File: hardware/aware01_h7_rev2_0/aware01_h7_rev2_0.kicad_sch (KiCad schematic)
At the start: 46 parts, among them J1 Conn_02x07_Odd_Even, J2 Conn_02x05_Odd_Even, SW3 PTS815, U1 LMR50410Y5FQDBVRQ1, U2 LM1117MP-3.3, U4 STM32H7A3RITx, U5 LM4040DIM3X-10, Y1 WE-XTAL 24.0MHz 50ppm

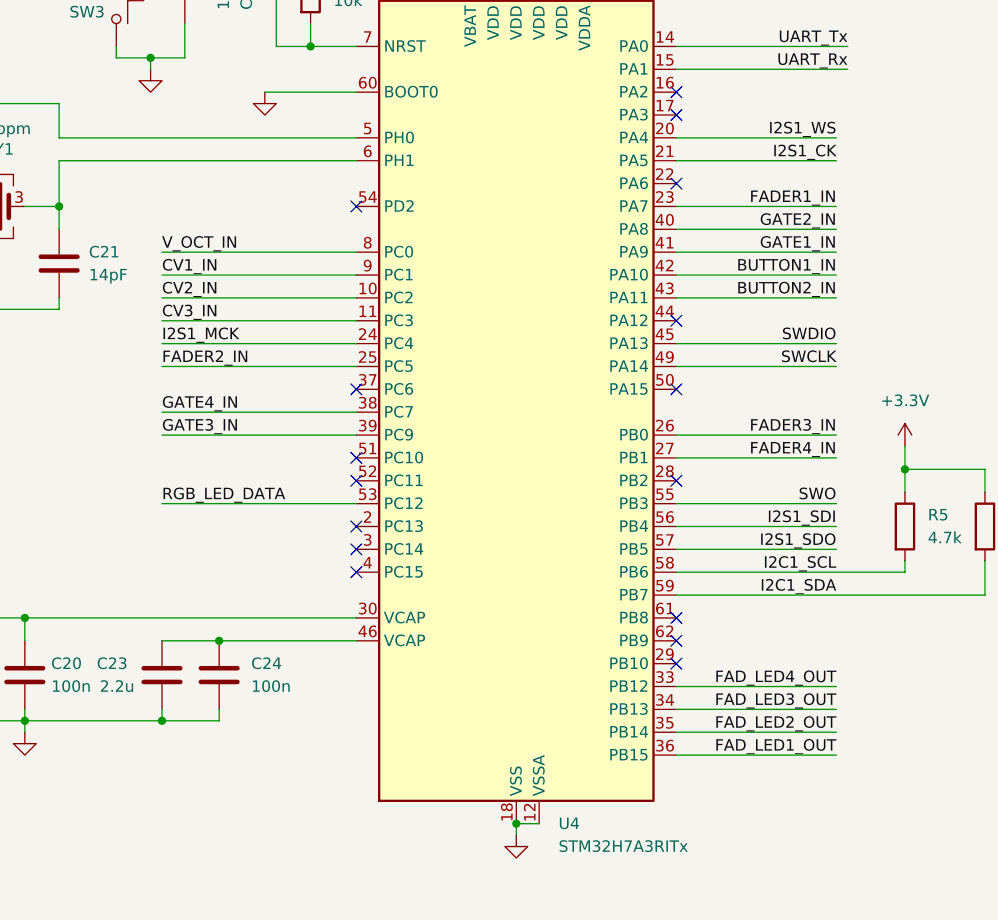
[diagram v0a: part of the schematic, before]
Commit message: feat: fixes in pcb design
- use correct BAT54S placement/layout
- fix pin mapping of fade potentiometers, also adjust routing
- switch pins that did not support PWM out (for fader led)
- switch pins that did not support EXTI
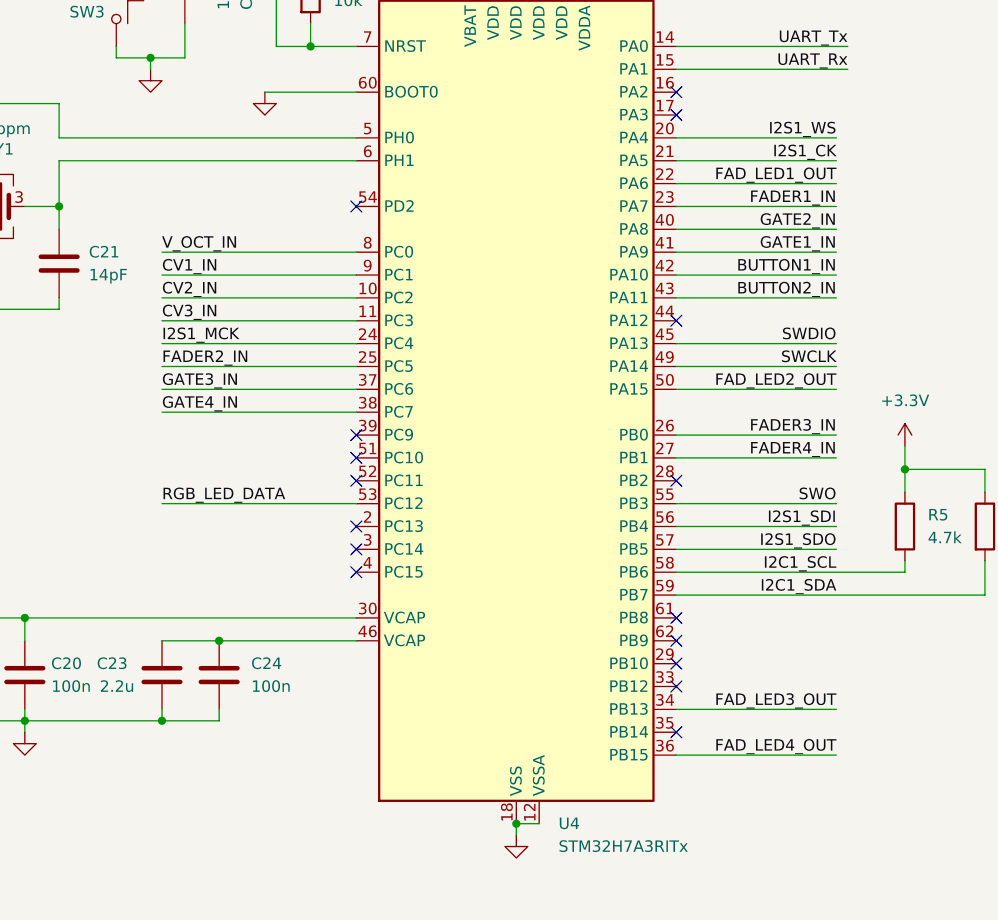
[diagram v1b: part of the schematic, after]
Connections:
- net FAD_LED1_OUT: now also U4.22 (PA6); no longer U4.36 (PB15)
- net FAD_LED2_OUT: now also U4.50 (PA15); no longer U4.35 (PB14)
- net FAD_LED4_OUT: now also U4.36 (PB15); no longer U4.33 (PB12)
- net GATE3_IN: now also U4.37 (PC6); no longer U4.39 (PC9)
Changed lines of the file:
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@@
+	)
+	(no_connect
+		(at 200.66 156.21)
 	)
 	(no_connect
@@
 	)
 	(no_connect
-		(at 236.22 128.27)
-	)
-	(no_connect
 		(at 64.77 237.49)
 	)
@@
 	)
 	(no_connect
+		(at 236.22 176.53)
+	)
+	(no_connect
 		(at 236.22 120.65)
 	)
@@
 	)
 	(no_connect
-		(at 236.22 181.61)
-	)
-	(no_connect
 		(at 236.22 143.51)
 	)
@@
 	)
 	(no_connect
-		(at 236.22 176.53)
+		(at 236.22 184.15)
 	)
 	(no_connect
@@
 	)
 	(no_connect
-		(at 236.22 151.13)
+		(at 236.22 189.23)
+	)
+	(no_connect
+		(at 236.22 181.61)
 	)
 	(no_connect
@@
 	)
 	(no_connect
-		(at 200.66 151.13)
-	)
-	(no_connect
 		(at 200.66 130.81)
 	)
@@
 	(wire
 		(pts
-			(xy 179.07 156.21) (xy 200.66 156.21)
-		)
-		(stroke
-			(width 0)
-			(type default)
-		)
-	)
-	(wire
-		(pts
 			(xy 46.99 40.64) (xy 34.29 40.64)
 		)
@@
 	(wire
 		(pts
+			(xy 179.07 151.13) (xy 200.66 151.13)
+		)
+		(stroke
+			(width 0)
+			(type default)
+		)
+	)
+	(wire
+		(pts
 			(xy 105.41 245.11) (xy 105.41 247.65)
 		)
@@
 	(wire
 		(pts
+			(xy 254 191.77) (xy 236.22 191.77)
+		)
+		(stroke
+			(width 0)
+			(type default)
+		)
+	)
+	(wire
+		(pts
 			(xy 34.29 48.26) (xy 34.29 50.8)
 		)
@@
 	(wire
 		(pts
+			(xy 254 128.27) (xy 236.22 128.27)
+		)
+		(stroke
+			(width 0)
+			(type default)
+		)
+	)
+	(wire
+		(pts
 			(xy 127 39.37) (xy 127 41.91)
 		)
@@
 	(wire
 		(pts
-			(xy 254 191.77) (xy 236.22 191.77)
-		)
-		(stroke
-			(width 0)
-			(type default)
-		)
-	)
-	(wire
-		(pts
 			(xy 48.26 245.11) (xy 52.07 245.11)
 		)
@@
 	(wire
 		(pts
+			(xy 254 151.13) (xy 236.22 151.13)
+		)
+		(stroke
+			(width 0)
+			(type default)
+		)
+	)
+	(wire
+		(pts
 			(xy 236.22 115.57) (xy 255.27 115.57)
 		)
@@
 	(wire
 		(pts
-			(xy 254 189.23) (xy 236.22 189.23)
-		)
-		(stroke
-			(width 0)
-			(type default)
-		)
-	)
-	(wire
-		(pts
 			(xy 133.35 41.91) (xy 127 41.91)
 		)
@@
 		(pts
 			(xy 105.41 252.73) (xy 105.41 250.19)
-		)
-		(stroke
-			(width 0)
-			(type default)
-		)
-	)
-	(wire
-		(pts
-			(xy 254 184.15) (xy 236.22 184.15)
 		)
 		(stroke
@@
 		)
 	)
+	(label "FAD_LED1_OUT"
+		(at 254 128.27 180)
+		(effects
+			(font
+				(size 1.27 1.27)
+			)
+			(justify right bottom)
+		)
+	)
+	(label "GATE3_IN"
+		(at 179.07 151.13 0)
+		(effects
+			(font
+				(size 1.27 1.27)
+			)
+			(justify left bottom)
+		)
+	)
 	(label "FAD_LED3_OUT"
 		(at 336.55 125.73 0)
@@
 		)
 	)
-	(label "GATE3_IN"
-		(at 179.07 156.21 0)
-		(effects
-			(font
-				(size 1.27 1.27)
-			)
-			(justify left bottom)
-		)
-	)
-	(label "FAD_LED1_OUT"
+	(label "FAD_LED4_OUT"
 		(at 254 191.77 180)
 		(effects
@@
 		)
 	)
-	(label "FAD_LED4_OUT"
-		(at 254 184.15 180)
-		(effects
-			(font
-				(size 1.27 1.27)
-			)
-			(justify right bottom)
-		)
-	)
 	(label "CV2_IN"
 		(at 179.07 140.97 0)
@@
 		)
 	)
-	(label "FAD_LED2_OUT"
-		(at 254 189.23 180)
-		(effects
-			(font
-				(size 1.27 1.27)
-			)
-			(justify right bottom)
-		)
-	)
 	(label "V_OCT_IN"
 		(at 336.55 62.23 0)
@@
 		(effects
 			(font
+				(size 1.27 1.27)
+			)
+			(justify right bottom)
+		)
+	)
+	(label "FAD_LED2_OUT"
+		(at 254 151.13 180)
+		(effects
+			(font
